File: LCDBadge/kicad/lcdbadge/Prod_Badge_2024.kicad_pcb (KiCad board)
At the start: 2 copper layers, 100 x 100 mm, 7 parts

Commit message: Add files via upload
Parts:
- removed the G*** at (0.00, 0.00) (x7)
- added BT1: Battery, Eagle_Plasic_Devices:12BHC186P1-GR, B.Cu at (85.5, 114.2)
- added G*** (x7): LOGO, LOGO, F.Cu at (84.1, 74.4)
- added R1: 0, Resistor_SMD:R_0805_2012Metric_Pad1.20x1.40mm_HandSolder, F.Cu at (67.9, 74.6)
- added R10: 10k, Resistor_SMD:R_0805_2012Metric_Pad1.20x1.40mm_HandSolder, F.Cu at (184.0, 68.4)
- added R11: 10k, Resistor_SMD:R_0805_2012Metric_Pad1.20x1.40mm_HandSolder, F.Cu at (184.0, 71.4)
- added R2: 0, Resistor_SMD:R_0805_2012Metric_Pad1.20x1.40mm_HandSolder, F.Cu at (166.2, 45.5)
- added R3: 0, Resistor_SMD:R_0805_2012Metric_Pad1.20x1.40mm_HandSolder, F.Cu at (179.2, 65.5)
- added R4: 0, Resistor_SMD:R_0805_2012Metric_Pad1.20x1.40mm_HandSolder, F.Cu at (179.2, 68.4)
- added R5: 0, Resistor_SMD:R_0805_2012Metric_Pad1.20x1.40mm_HandSolder, F.Cu at (179.2, 71.4)
- added R6: 0, Resistor_SMD:R_0805_2012Metric_Pad1.20x1.40mm_HandSolder, F.Cu at (179.2, 74.3)
- added R7: 0, Resistor_SMD:R_0805_2012Metric_Pad1.20x1.40mm_HandSolder, F.Cu at (110.5, 74.6)
- added R8: 10k, Resistor_SMD:R_0805_2012Metric_Pad1.20x1.40mm_HandSolder, F.Cu at (180.7, 59.2)
- added R9: 10k, Resistor_SMD:R_0805_2012Metric_Pad1.20x1.40mm_HandSolder, F.Cu at (184.0, 65.5)
- added REF**: MountingHole_4.3mm_M4, MountingHole:MountingHole_4.3mm_M4, F.Cu at (42.5, 32.1)
- added REF**: MountingHole_4.3mm_M4, MountingHole:MountingHole_4.3mm_M4, F.Cu at (128.0, 31.7)
- added SW1: SW_Push, Button_Switch_THT:SW_Tactile_Straight_KSA0Axx1LFTR, F.Cu at (39.4, 89.7)
- added SW2: SW_Push, Button_Switch_THT:SW_Tactile_Straight_KSA0Axx1LFTR, F.Cu at (51.1, 89.7)
- added SW3: SW_Push, Button_Switch_THT:SW_Tactile_Straight_KSA0Axx1LFTR, F.Cu at (123.8, 82.0)
- added SW4: SW_Push, Button_Switch_THT:SW_Tactile_Straight_KSA0Axx1LFTR, F.Cu at (123.8, 92.9)
- added U1: ~, Seeed_Studio:MOUDLE14P-SMD-2.54-21X17.8MM_BAT, F.Cu at (39.0, 80.4)
- added U2: ~, TFT:AliExpress_1.8_128x160_ST7735, F.Cu at (89.1, 70.7)
- added X1: Badgelife_sao_connector_v169bis, Badgelife:Badgelife-SAOv169-BADGE-2x3, F.Cu at (114.0, 32.5)
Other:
- net class Default removed

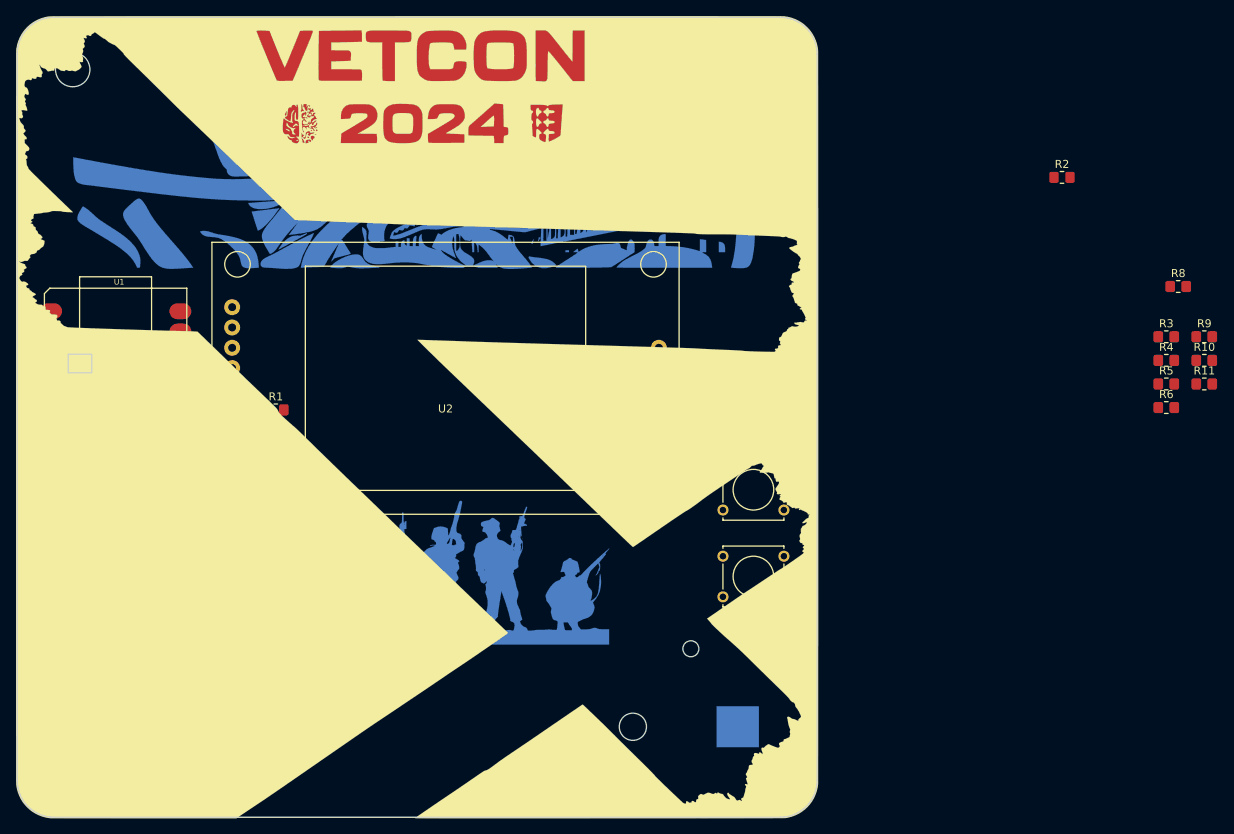
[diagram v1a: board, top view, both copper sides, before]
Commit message: routed board updated button changed from route to large vias for module
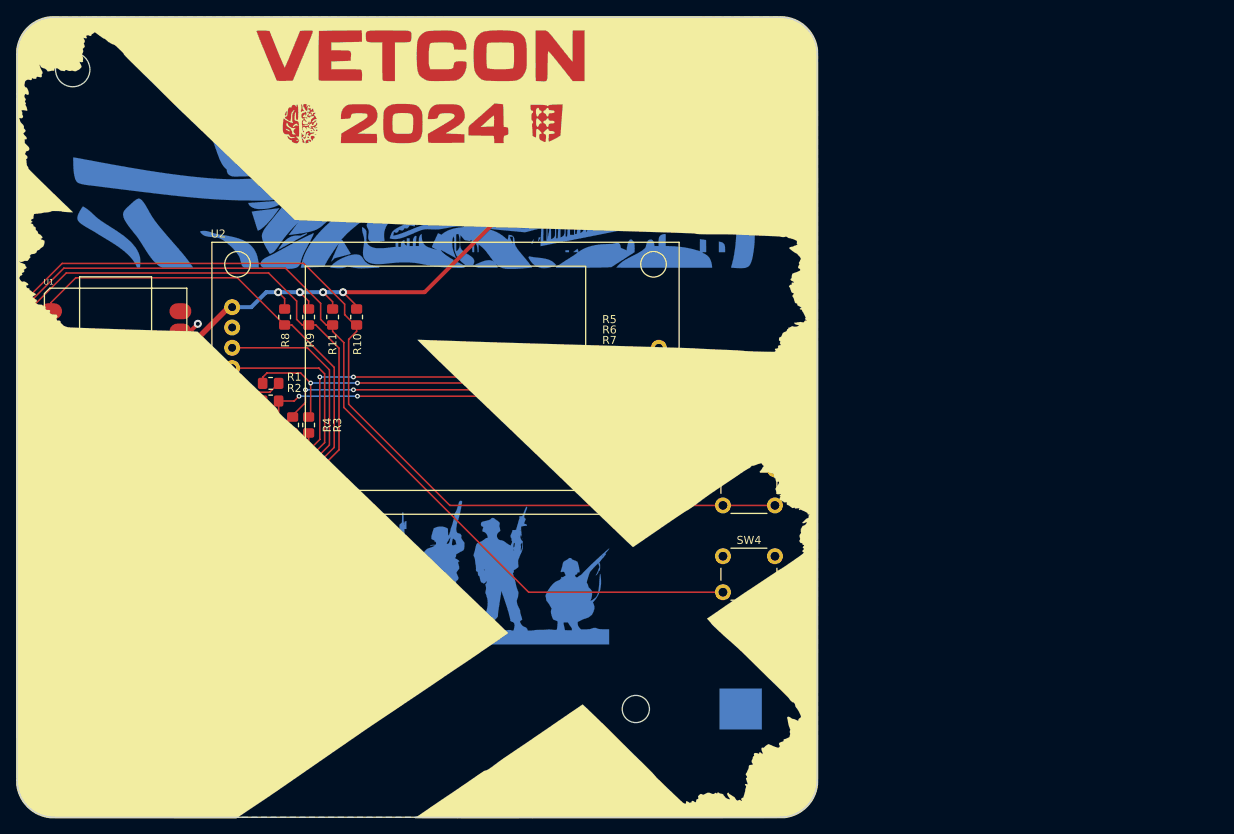
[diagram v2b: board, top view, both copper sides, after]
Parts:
- SW1, SW2, SW3, SW4: footprint Button_Switch_THT:SW_Tactile_Straight_KSA0Axx1LFTR -> Button_Switch_THT:SW_PUSH_6mm_H4.3mm
- moved R9 112.0 mm to (72.0, 63.0), turned to 90 degrees
- moved R8 111.8 mm to (69.0, 63.0), turned to 90 degrees
- moved R4 109.5 mm to (70.0, 76.5), turned to 90 degrees
- moved R11 109.3 mm to (75.0, 63.0), turned to 90 degrees
- moved R3 107.8 mm to (72.0, 76.5), turned to 90 degrees
- moved R10 106.1 mm to (78.0, 63.0), turned to 90 degrees
- moved R2 102.8 mm to (67.2, 73.5)
- moved R6 69.6 mm to (109.6, 72.5), turned to 180 degrees
- moved R5 69.6 mm to (109.6, 70.5)
- moved R1 3.37 mm to (67.2, 71.3), turned to 180 degrees
- moved BT1 2.25 mm to (85.9, 112.0), turned to 0 degrees
- moved R7 0.87 mm to (109.6, 74.6)
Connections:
- net Net-(BT1-+) renamed /BAT+
- BT1 pad 2: Net-(BT1--) -> GND
- R11 pad 1: /BUTTON_2 -> /BUTTON_4
- R8 pad 1: /BUTTON_4 -> /BUTTON_1
- R9 pad 1: /BUTTON_1 -> /BUTTON_2
- SW1 pad 2: /BUTTON_4 -> /BUTTON_1
- SW2 pad 2: /BUTTON_1 -> /BUTTON_2
- SW4 pad 2: /BUTTON_2 -> /BUTTON_4
- U1 pad 16: Net-(BT1--) -> GND
- U1 pad 3: /BUTTON_3 -> /BUTTON_4
- U1 pad 4: /BUTTON_4 -> /BUTTON_3
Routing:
- net /BUTTON_3: track 0.00 -> 126.3 mm
- net /BUTTON_4: track 0.00 -> 118.8 mm
- net +3V3: track 0.00 -> 98.9 mm, vias 0 -> 4
- net /BUTTON_1: track 0.00 -> 94.4 mm
- net /BUTTON_2: track 0.00 -> 92.8 mm
- net /SD_CS: track 0.00 -> 92.1 mm, vias 0 -> 2
- net /SCK: track 0.00 -> 68.7 mm, vias 0 -> 2
- net /TFT_CS: track 0.00 -> 62.9 mm
- net /TFT_RESET: track 0.00 -> 60.7 mm
- net /BAT+: track 0.00 -> 49.8 mm
- net /MOSI: track 0.00 -> 48.5 mm, vias 0 -> 2
- net /MISO: track 0.00 -> 44.1 mm, vias 0 -> 2
- net Net-(U1-TOUCH9_GPIO9_MOSI_A10_D10): track 0.00 -> 36.9 mm
- net Net-(U1-TOUCH8_GPIO8_MISO_A9_D9): track 0.00 -> 30.4 mm
- net /TFT_A0: track 0.00 -> 10.8 mm, vias 0 -> 1
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- added copper zone on B.Cu, net /BAT+
- added copper zone on B.Cu, net GND

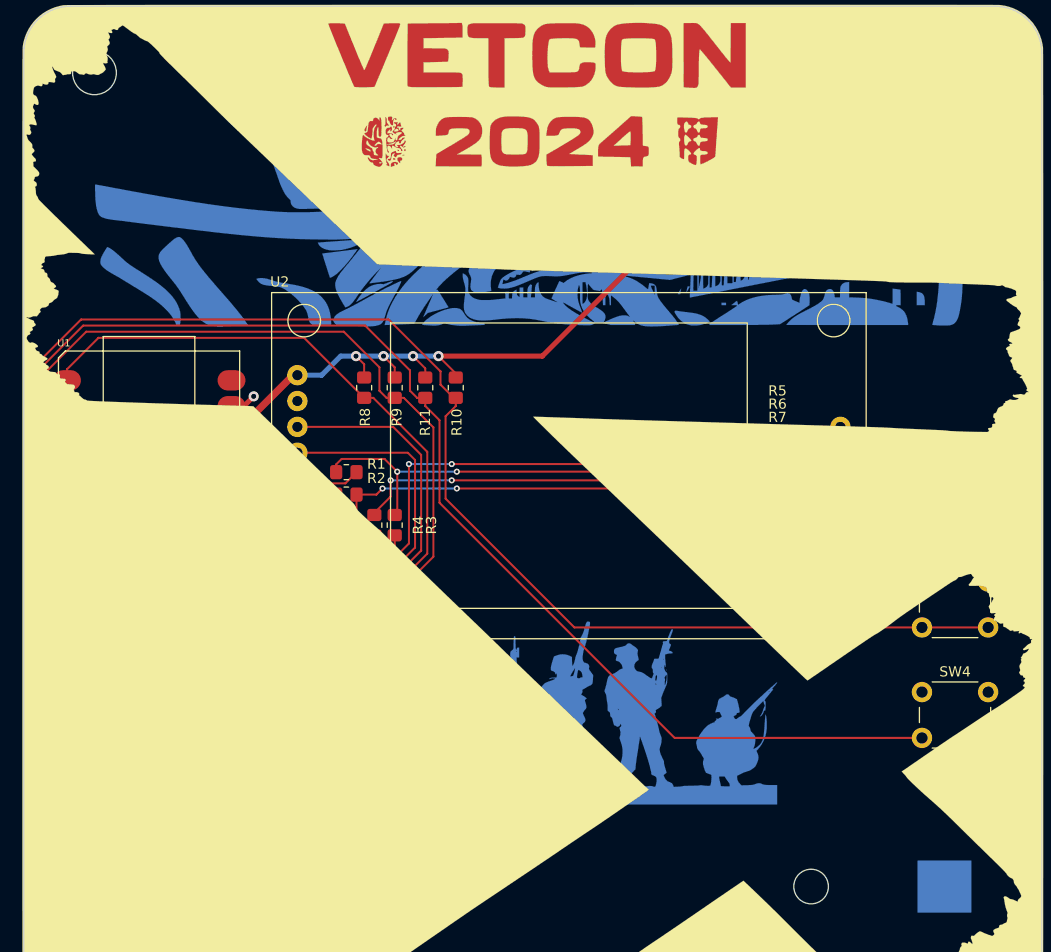
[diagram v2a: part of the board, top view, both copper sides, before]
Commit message: rotated esp moved resistors away from sd card holder
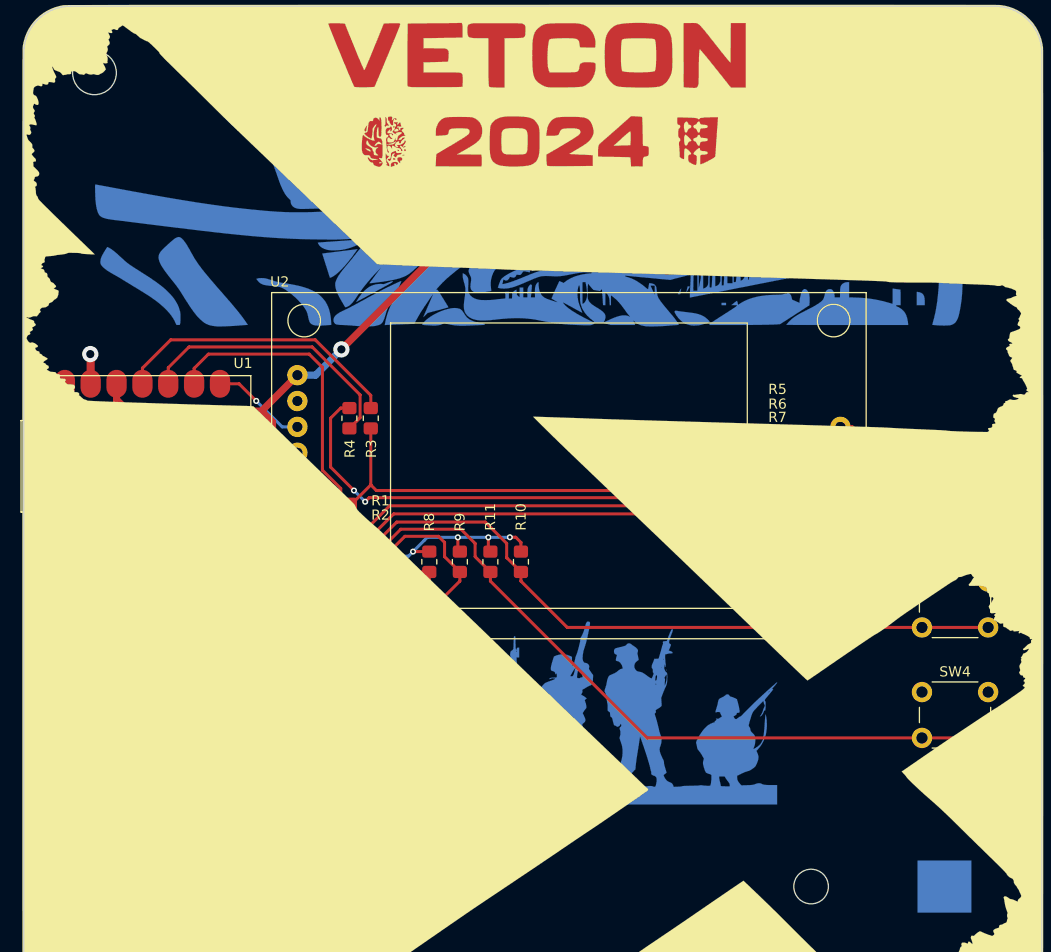
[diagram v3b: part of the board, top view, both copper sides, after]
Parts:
- moved U1 18.8 mm to (57.7, 79.6), turned to 90 degrees
- moved R10 18.3 mm to (84.4, 80.1)
- moved R11 18.3 mm to (81.4, 80.1)
- moved R8 18.3 mm to (75.4, 80.1)
- moved R9 18.3 mm to (78.4, 80.1)
- moved R4 10.8 mm to (67.5, 66.0)
- moved R3 10.8 mm to (69.7, 66.0), turned to -90 degrees
- moved G*** 7.17 mm to (78.6, 79.0)
- moved R2 3.54 mm to (66.7, 77.0)
- moved R1 3.25 mm to (66.7, 74.5), turned to 0 degrees
- moved R5 0.15 mm to (109.6, 70.3)
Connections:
- U1 pad 7: /TFT_CS -> /TFT_A0
- U1 pad 8: /TFT_A0 -> /TFT_CS
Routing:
- net /TFT_CS: track 62.9 -> 9.35 mm, vias 0 -> 1
- net /TFT_RESET: track 60.7 -> 15.5 mm, vias 0 -> 1
- net /BUTTON_3: track 126.3 -> 93.5 mm
- net +3V3: track 98.9 -> 130.8 mm, vias 4 -> 5
- net /BUTTON_4: track 118.8 -> 100.5 mm
- net /BUTTON_2: track 92.8 -> 77.1 mm
- net /BUTTON_1: track 94.4 -> 82.3 mm
- net /MISO: track 44.1 -> 54.9 mm
- net /SD_CS: track 92.1 -> 83.3 mm, vias 2 -> 0
- net Net-(U1-TOUCH9_GPIO9_MOSI_A10_D10): track 36.9 -> 28.6 mm
- net /BAT+: track 49.8 -> 42.4 mm
- net /SCK: track 68.7 -> 74.3 mm, vias 2 -> 0
- net Net-(U2-SDA): track 7.12 -> 3.27 mm
- net Net-(U1-TOUCH8_GPIO8_MISO_A9_D9): track 30.4 -> 26.9 mm
- net Net-(U2-SCK): track 5.26 -> 3.26 mm
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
